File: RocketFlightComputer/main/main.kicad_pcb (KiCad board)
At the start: 4 copper layers, 53.7 x 53.7 mm, 130 parts, among them J1 BATT, Q2 SI2302, Q3 SI2302, Q4 SI2302, Y1 32.768kHz, Y2 24MHz, Y3 32.768kHz, Y4 32.768kHz

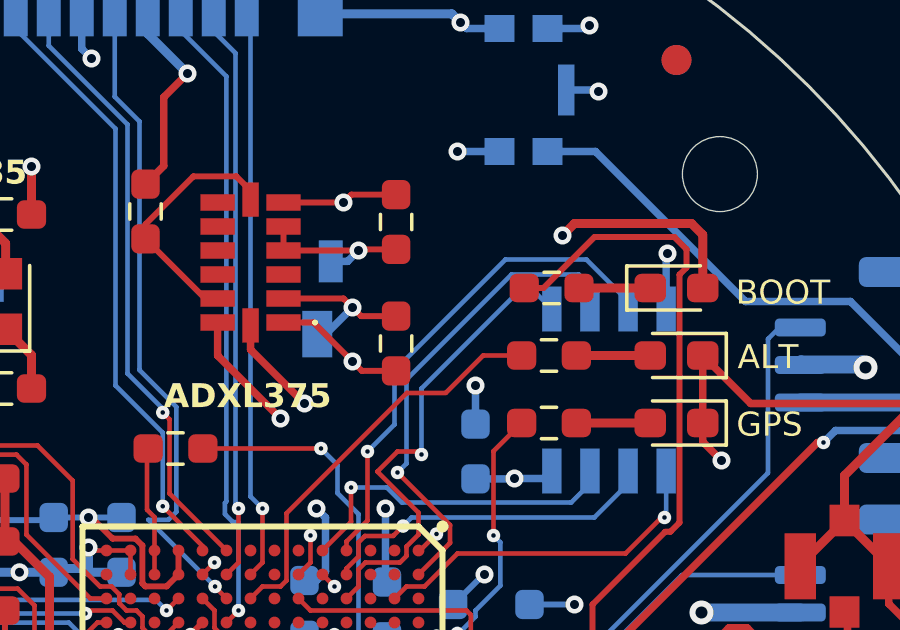
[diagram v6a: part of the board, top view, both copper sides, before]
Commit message: PR1; Fix PSRAM length of data, clock and cs pins to match since high speed data transmission, needs to be within 0.5mm trace length delta
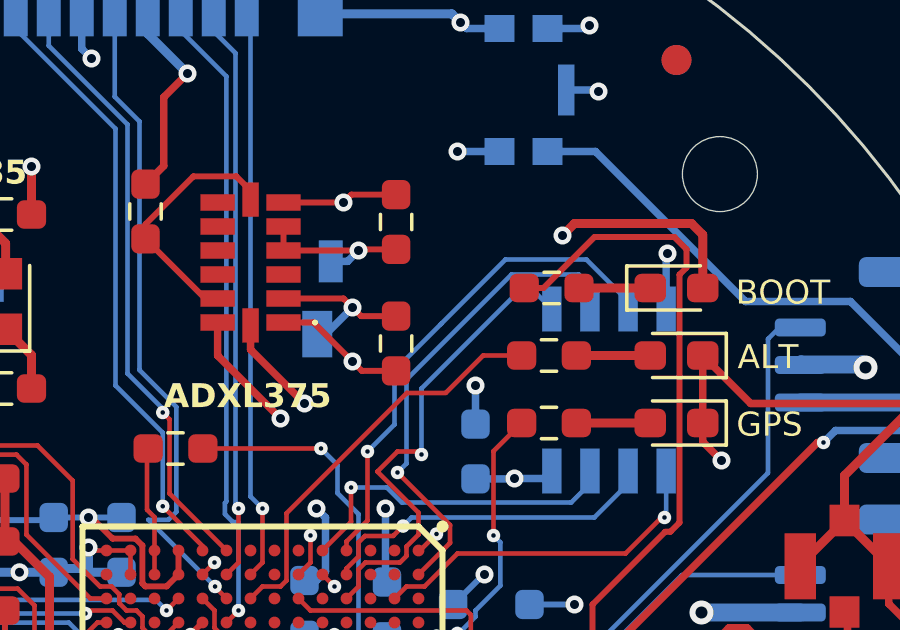
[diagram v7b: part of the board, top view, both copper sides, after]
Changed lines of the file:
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@@
 	)
 	(segment
-		(start 125.768 44.093)
-		(end 125.768 43.833)
+		(start 121.683 42.443)
+		(end 119.543576 44.582424)
 		(width 0.155)
 		(layer "B.Cu")
@@
 	)
 	(segment
-		(start 121.683 42.443)
-		(end 117.983 46.143)
+		(start 124.378 42.443)
+		(end 121.683 42.443)
 		(width 0.155)
 		(layer "B.Cu")
@@
 	)
 	(segment
-		(start 117.983 47.943)
-		(end 117.083 48.843)
+		(start 125.768 44.093)
+		(end 125.768 43.833)
 		(width 0.155)
 		(layer "B.Cu")
@@
 	)
 	(segment
-		(start 124.378 42.443)
-		(end 121.683 42.443)
+		(start 119.543576 44.582424)
+		(end 119.532382 44.593618)
+		(width 0.155)
+		(layer "B.Cu")
+		(net 69)
+	)
+	(segment
+		(start 117.983 47.943)
+		(end 117.083 48.843)
+		(width 0.155)
+		(layer "B.Cu")
+		(net 69)
+	)
+	(segment
+		(start 119.532382 44.593618)
+		(end 117.983 46.143)
 		(width 0.155)
 		(layer "B.Cu")
@@
 	)
 	(generated
+		(type tuning_pattern)
+		(name "Tuning Pattern")
+		(layer "B.Cu")
+		(base_line
+			(pts
+				(xy 119.543576 44.582424) (xy 119.532382 44.593618)
+			)
+		)
+		(corner_radius_percent 80)
+		(end
+			(xy 119.532382 44.593618)
+		)
+		(initial_side "left")
+		(last_diff_pair_gap 0.18)
+		(last_netname "/EMC_28")
+		(last_status "tuned")
+		(last_track_width 0.155)
+		(last_tuning "18.3457 mm (tuned)")
+		(max_amplitude 1)
+		(min_amplitude 0.2)
+		(min_spacing 0.6)
+		(origin
+			(xy 119.543576 44.582424)
+		)
+		(override_custom_rules no)
+		(rounded yes)
+		(single_sided no)
+		(target_length 1000000)
+		(target_length_max 1000000)
+		(target_length_min 0)
+		(target_skew 0)
+		(target_skew_max 0.1)
+		(target_skew_min -0.1)
+		(tuning_mode "single")
+		(members aef0a5aa-b48c-4624-99af-37c13308d2ee)
+	)
+	(generated

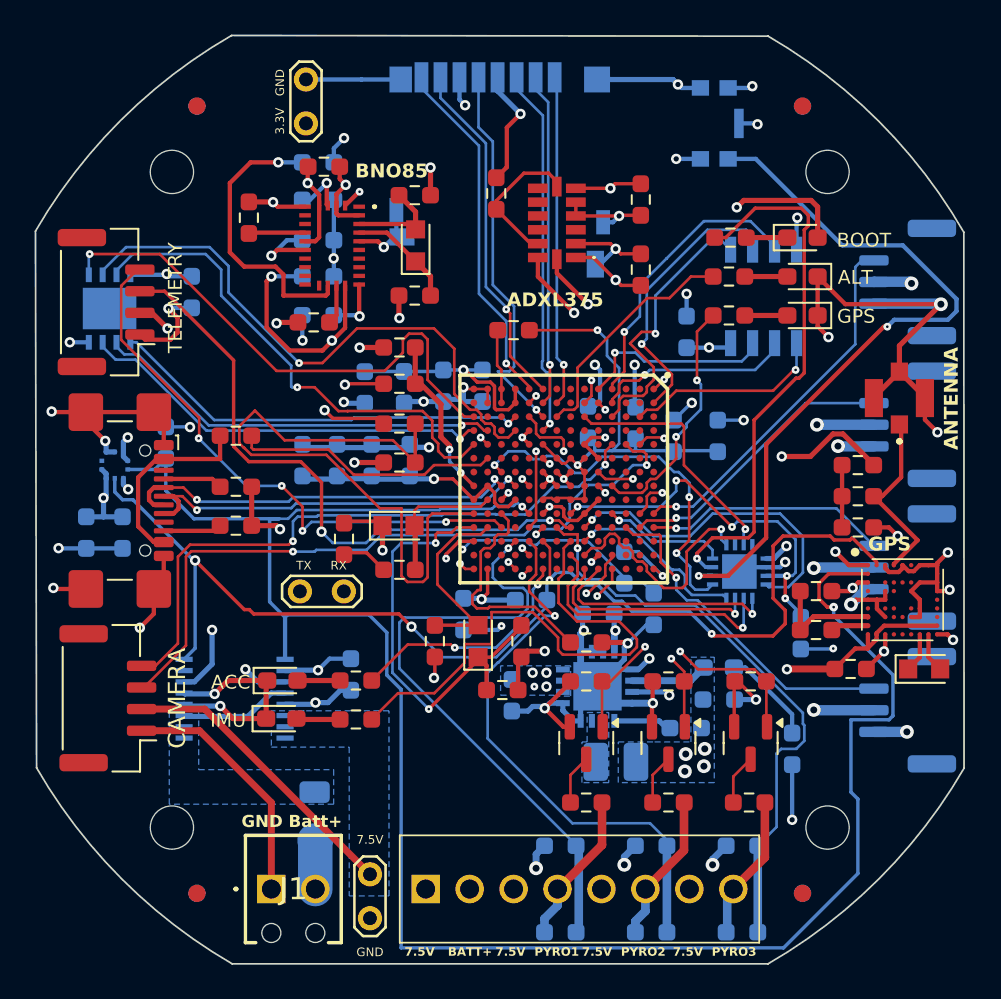
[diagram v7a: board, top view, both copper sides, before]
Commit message: First pass of verification and validation of pcb design
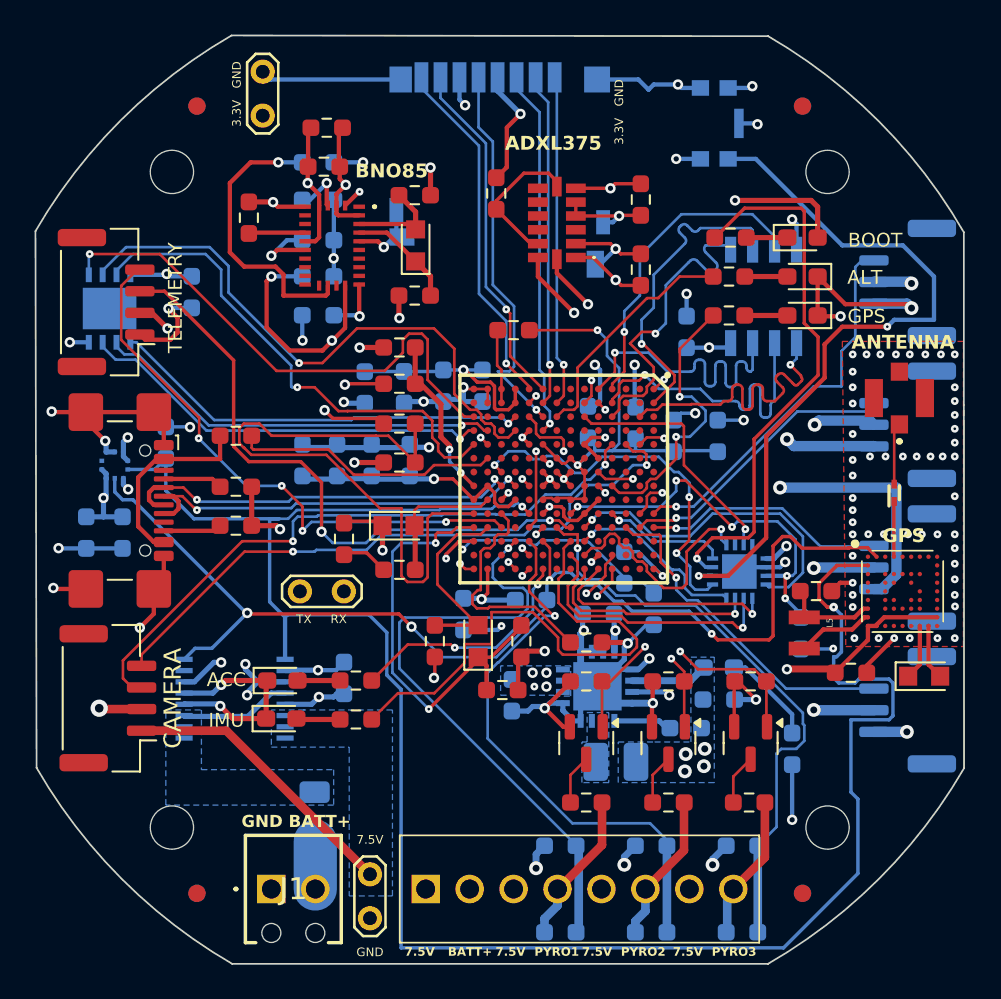
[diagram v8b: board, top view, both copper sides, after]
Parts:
- removed FB1: 120ohm, Resistor_SMD:R_0603_1608Metric_Pad0.98x0.95mm_HandSolder
- removed R13: 10OHM-0603-1/10W-1%, Resistor_SMD:R_0603_1608Metric_Pad0.98x0.95mm_HandSolder
- removed R35: 10k, Resistor_SMD:R_0603_1608Metric_Pad0.98x0.95mm_HandSolder
- added D5: ESD9R3.3ST5G, footprint:ESD9R3_3ST5G, F.Cu at (132.7, 58.1)
- C37: value 47PF-0603-50V-5% -> 0.1uF
- L5: footprint Resistor_SMD:R_0603_1608Metric_Pad0.98x0.95mm_HandSolder -> ZOE-M8Q:0806
- R2, R33, R5, R7, R8: value 470 -> 1k
- moved C37 38.4 mm to (99.9, 37.0), turned to 180 degrees
- moved TP1 2.54 mm to (96.2, 36.3)
- moved L5 0.89 mm to (127.5, 66.6), turned to -90 degrees
- moved U-BLOX_ZOE_M8Q-0-10 0.48 mm to (133.2, 63.8)
- moved C40 0.45 mm to (100.9, 68.8)
- moved Y4 0.42 mm to (134.4, 68.7)
- moved C39 0.22 mm to (130.2, 68.5)
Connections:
- BNO85 pad 18: Net-(BNO85-H_CSN) -> unconnected-(BNO85-H_CSN-Pad18)
- C37 pad 1: Net-(C37-Pad1) -> +3.3V
- CONMHF1-SMD-G-T1 pad 1: /GPS ZOEM8/ANT -> Net-(CONMHF1-SMD-G-T1-SIGNAL)
- S4B-PH-K-S_LF__SN_1 pad 1: GNDREF -> +3.3V
- S4B-PH-K-S_LF__SN_1 pad 2: +3.3V -> GNDREF
- S4B-PH-K-S_LF__SN_1 pad 3: /Xbee_RX -> /Xbee_TX
- S4B-PH-K-S_LF__SN_1 pad 4: /Xbee_TX -> /Xbee_RX
- S4B-PH-K-S_LF__SN_2 pad 1: GNDREF -> +7.5V
- S4B-PH-K-S_LF__SN_2 pad 2: +7.5V -> GNDREF
- S4B-PH-K-S_LF__SN_2 pad 3: /Cam_TX -> /Cam_RX
- S4B-PH-K-S_LF__SN_2 pad 4: /Cam_RX -> /Cam_TX
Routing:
- net GNDREF: track 297.4 -> 272.2 mm, vias 83 -> 130
- net +3.3V: track 102.1 -> 94.0 mm, vias 31 -> 28
- net /GPS ZOEM8/ANT: track 10.7 -> 3.20 mm
- net /EMC_29: track 11.3 -> 18.3 mm
- net /EMC_25: track 11.5 -> 18.3 mm
- net /EMC_26: track 11.7 -> 18.4 mm
- net Net-(C37-Pad1): track 3.60 -> 0.00 mm
- net Net-(CONMHF1-SMD-G-T1-SIGNAL): track 0.00 -> 3.57 mm
- net /Cam_TX: track 40.3 -> 37.1 mm
- net /BMP390_SCL1: track 113.1 -> 115.8 mm
- net Net-(BNO85-H_CSN): track 2.29 -> 0.00 mm
- net Net-(U-BLOX_ZOE_M8Q-0-10-V_DCDC_OUT): track 2.19 -> 4.43 mm
- net /EMC_27: track 16.3 -> 18.4 mm
- net /BMP390_SDA1: track 68.3 -> 66.3 mm
- net /EMC_24: track 16.4 -> 18.4 mm
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- added copper zone on F.Cu, net GNDREF
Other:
- board text added: "GND BATT+"
- board text removed: "GND Batt+"
